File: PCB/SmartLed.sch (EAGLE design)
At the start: 49 parts, among them IC2 DS1307, IC3 MEGA8-P, K1 G5LE, Q2 32.768khz, T1 BC337

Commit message: Refactor PCB design (several enhancements)
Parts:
- removed IC4: (no value), v-reg:78XXS
- removed LED4: (no value), led:LED3MM
- removed R9: 330, rcl:R-EU_0207/10
- added IC1: (no value), v-reg:79XXL
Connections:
- removed net N$19: LED4.A, R9.1
- net +12V: now also IC1.IN; no longer IC4.IN
- net +5V: now also IC1.OUT; no longer IC4.OUT
- net GND: now also IC1.GND; no longer IC4.GND
- net N$6: no longer R9.2
- net N$7: no longer LED4.C
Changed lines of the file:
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@@
 <part name="R8" library="rcl" deviceset="R-EU_" device="0207/10" value="1.2k"/>
 <part name="GND10" library="supply1" deviceset="GND" device=""/>
-<part name="LED4" library="led" deviceset="LED" device="3MM"/>
-<part name="R9" library="rcl" deviceset="R-EU_" device="0207/10" value="330"/>
 <part name="LED5" library="led" deviceset="LED" device="3MM"/>
 <part name="R10" library="rcl" deviceset="R-EU_" device="0207/10" value="330"/>
@@
 <part name="C2" library="rcl" deviceset="C-EU" device="025-025X050" value="100nf"/>
 <part name="C7" library="rcl" deviceset="CPOL-EU" device="E2.5-5" value="4.7uf"/>
-<part name="IC4" library="v-reg" deviceset="78XXS" device=""/>
 <part name="GND8" library="supply1" deviceset="GND" device=""/>
 <part name="JP1" library="pinhead" deviceset="PINHD-1X5" device=""/>
@@
 <part name="P+11" library="supply1" deviceset="+5V" device=""/>
 <part name="Q2" library="crystal" deviceset="CRYSTAL" device="TC26V" value="32.768khz"/>
+<part name="IC1" library="v-reg" deviceset="79XXL" device=""/>
 </parts>
 <sheets>
@@
 <instance part="R8" gate="G$1" x="254" y="53.34"/>
 <instance part="GND10" gate="1" x="276.86" y="50.8"/>
-<instance part="LED4" gate="G$1" x="-73.66" y="73.66" rot="R270"/>
-<instance part="R9" gate="G$1" x="-63.5" y="73.66"/>
 <instance part="LED5" gate="G$1" x="190.5" y="15.24" rot="R90"/>
 <instance part="R10" gate="G$1" x="180.34" y="15.24"/>
@@
 <instance part="C2" gate="G$1" x="175.26" y="172.72" rot="MR180"/>
 <instance part="C7" gate="G$1" x="40.64" y="78.74" rot="R180"/>
-<instance part="IC4" gate="1" x="-5.08" y="111.76"/>
 <instance part="GND8" gate="1" x="175.26" y="165.1"/>
 <instance part="JP1" gate="A" x="132.08" y="35.56"/>
@@
 <instance part="P+11" gate="1" x="68.58" y="177.8"/>
 <instance part="Q2" gate="G$1" x="182.88" y="154.94" rot="R90"/>
+<instance part="IC1" gate="A" x="-5.08" y="111.76" rot="MR180"/>
 </instances>
 <busses>
@@
 <pinref part="OK1" gate="A" pin="A"/>
 <wire x1="-53.34" y1="58.42" x2="-53.34" y2="60.96" width="0.1524" layer="91"/>
-<wire x1="-53.34" y1="60.96" x2="-58.42" y2="60.96" width="0.1524" layer="91"/>
-<pinref part="R9" gate="G$1" pin="2"/>
-<wire x1="-58.42" y1="60.96" x2="-63.5" y2="60.96" width="0.1524" layer="91"/>
-<wire x1="-58.42" y1="73.66" x2="-58.42" y2="60.96" width="0.1524" layer="91"/>
+<wire x1="-53.34" y1="60.96" x2="-63.5" y2="60.96" width="0.1524" layer="91"/>
 <junction x="-73.66" y="60.96"/>
 <junction x="-63.5" y="60.96"/>
-<junction x="-58.42" y="60.96"/>
 </segment>
 </net>
@@
 <pinref part="R5-0.25W" gate="G$1" pin="2"/>
 <wire x1="-63.5" y1="48.26" x2="-73.66" y2="48.26" width="0.1524" layer="91"/>
-<wire x1="-73.66" y1="48.26" x2="-78.74" y2="48.26" width="0.1524" layer="91"/>
-<wire x1="-78.74" y1="48.26" x2="-111.76" y2="48.26" width="0.1524" layer="91"/>
+<wire x1="-73.66" y1="48.26" x2="-111.76" y2="48.26" width="0.1524" layer="91"/>
 <wire x1="-111.76" y1="48.26" x2="-111.76" y2="55.88" width="0.1524" layer="91"/>
 <pinref part="B1" gate="1" pin="-"/>
@@
 <pinref part="OK1" gate="A" pin="C"/>
 <wire x1="-53.34" y1="48.26" x2="-53.34" y2="53.34" width="0.1524" layer="91"/>
-<pinref part="LED4" gate="G$1" pin="C"/>
-<wire x1="-78.74" y1="73.66" x2="-78.74" y2="48.26" width="0.1524" layer="91"/>
-<junction x="-78.74" y="48.26"/>
 <junction x="-63.5" y="48.26"/>
 </segment>
@@
 <pinref part="P+2" gate="1" pin="+5V"/>
 <wire x1="12.7" y1="119.38" x2="12.7" y2="111.76" width="0.1524" layer="91"/>
-<wire x1="12.7" y1="111.76" x2="2.54" y2="111.76" width="0.1524" layer="91"/>
-<pinref part="IC4" gate="1" pin="OUT"/>
+<pinref part="IC1" gate="A" pin="OUT"/>
+<wire x1="2.54" y1="111.76" x2="12.7" y2="111.76" width="0.1524" layer="91"/>
 </segment>
 <segment>
@@
 <pinref part="GND2" gate="1" pin="GND"/>
 <wire x1="-5.08" y1="104.14" x2="-5.08" y2="101.6" width="0.1524" layer="91"/>
-<pinref part="IC4" gate="1" pin="GND"/>
+<pinref part="IC1" gate="A" pin="GND"/>
 </segment>
 <segment>
@@
 <net name="+12V" class="1">
 <segment>
-<wire x1="-12.7" y1="111.76" x2="-20.32" y2="111.76" width="0.1524" layer="91"/>
 <pinref part="12V" gate="-1" pin="KL"/>
 <wire x1="-20.32" y1="111.76" x2="-33.02" y2="111.76" width="0.1524" layer="91"/>
@@
 <pinref part="P+6" gate="1" pin="+12V"/>
 <wire x1="-20.32" y1="119.38" x2="-20.32" y2="111.76" width="0.1524" layer="91"/>
-<junction x="-20.32" y="111.76"/>
-<pinref part="IC4" gate="1" pin="IN"/>
+<pinref part="IC1" gate="A" pin="IN"/>
+<wire x1="-20.32" y1="111.76" x2="-12.7" y2="111.76" width="0.1524" layer="91"/>
 </segment>
 <segment>
@@
 </segment>
 </net>
-<net name="N$19" class="0">
-<segment>
-<pinref part="R9" gate="G$1" pin="1"/>
-<pinref part="LED4" gate="G$1" pin="A"/>
-<wire x1="-68.58" y1="73.66" x2="-71.12" y2="73.66" width="0.1524" layer="91"/>
-</segment>
-</net>

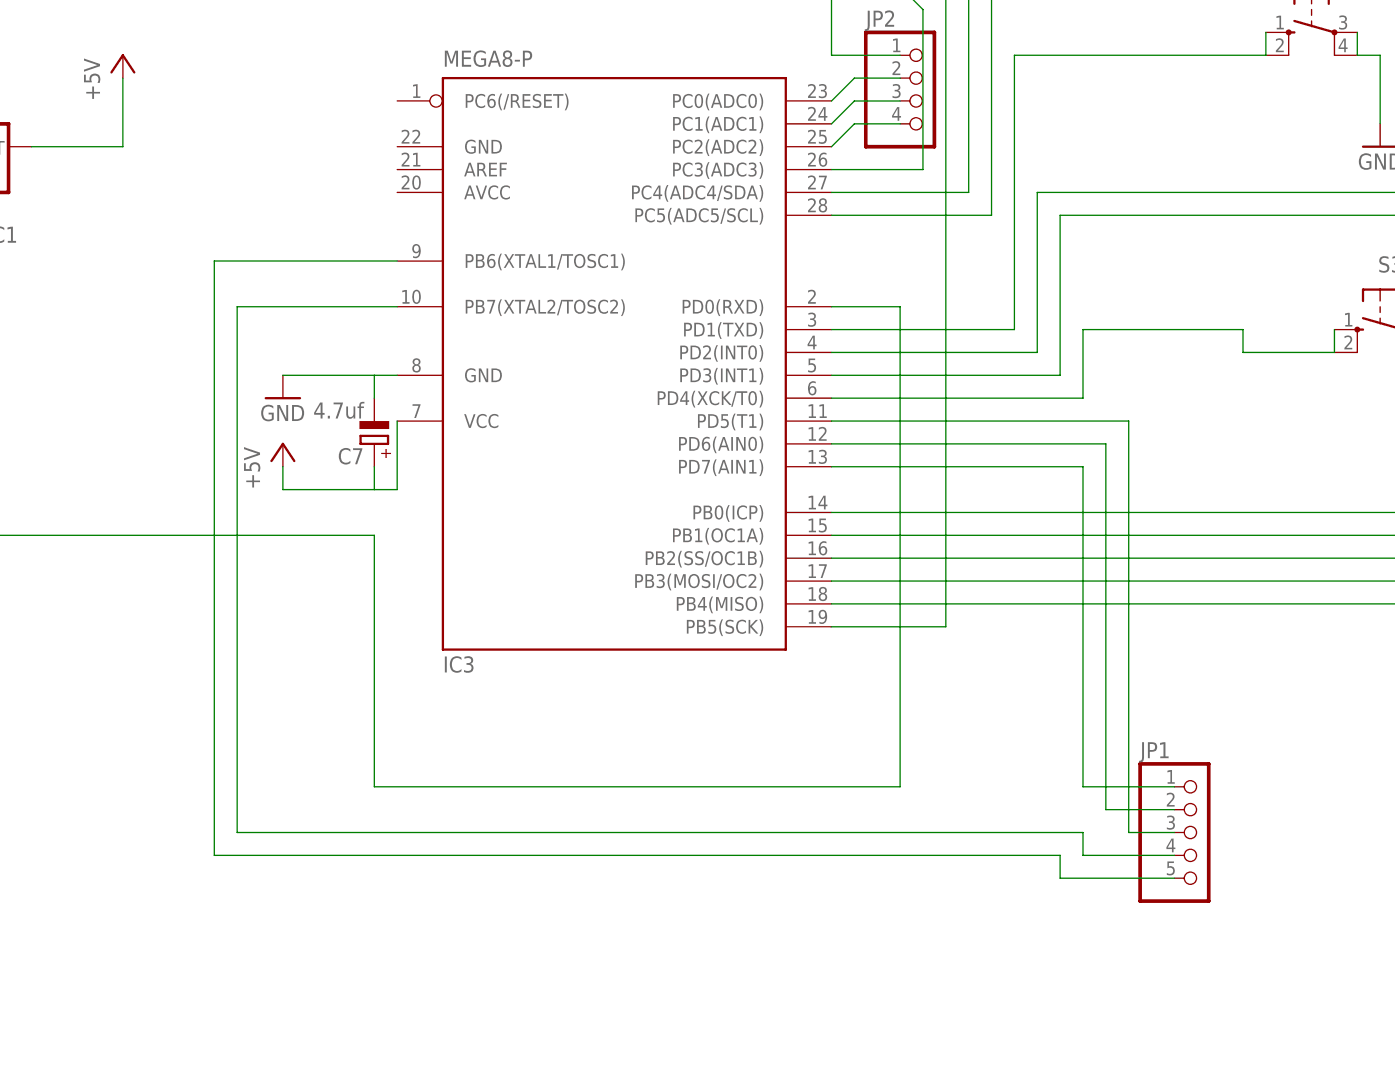
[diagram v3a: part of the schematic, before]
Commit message: Add PIR sensor pins to PCB
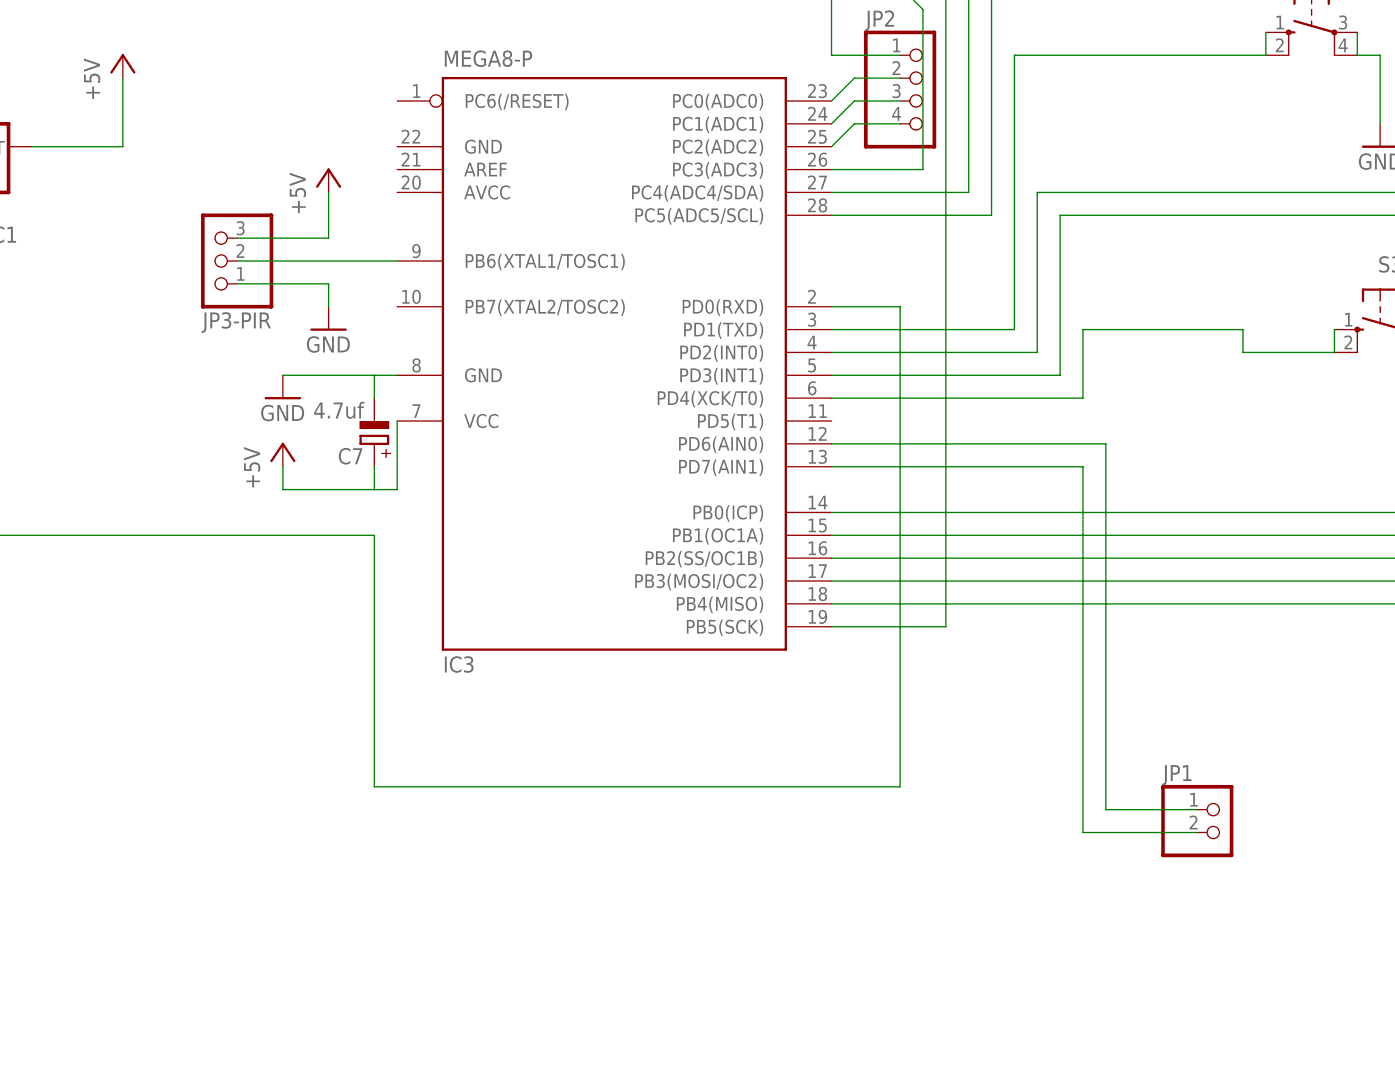
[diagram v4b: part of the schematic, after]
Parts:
- added JP3-PIR: (no value), pinhead:PINHD-1X3
- JP1: device pinhead:PINHD-1X5 -> pinhead:PINHD-1X2
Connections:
- removed net N$35: IC3.PD5(T1), JP1.3
- removed net N$41: IC3.PB6(XTAL1/TOSC1), JP1.5
- removed net N$42: IC3.PB7(XTAL2/TOSC2), JP1.4
- new net N$19: IC3.PB6(XTAL1/TOSC1), JP3-PIR.2
- net +5V: now also JP3-PIR.3
- net GND: now also JP3-PIR.1
- net N$37: now also JP1.1; no longer JP1.2
- net N$39: now also JP1.2; no longer JP1.1
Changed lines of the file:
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@@
 <part name="C7" library="rcl" deviceset="CPOL-EU" device="E2.5-5" value="4.7uf"/>
 <part name="GND8" library="supply1" deviceset="GND" device=""/>
-<part name="JP1" library="pinhead" deviceset="PINHD-1X5" device=""/>
 <part name="C1" library="rcl" deviceset="CPOL-EU" device="E2.5-5" value="4.7uf"/>
 <part name="C4" library="rcl" deviceset="C-EU" device="025-025X050" value="100nf"/>
@@
 <part name="Q2" library="crystal" deviceset="CRYSTAL" device="TC26V" value="32.768khz"/>
 <part name="IC1" library="v-reg" deviceset="79XXL" device=""/>
+<part name="JP3-PIR" library="pinhead" deviceset="PINHD-1X3" device=""/>
+<part name="P+12" library="supply1" deviceset="+5V" device=""/>
+<part name="GND17" library="supply1" deviceset="GND" device=""/>
+<part name="JP1" library="pinhead" deviceset="PINHD-1X2" device=""/>
 </parts>
 <sheets>
@@
 <instance part="C7" gate="G$1" x="40.64" y="78.74" rot="R180"/>
 <instance part="GND8" gate="1" x="175.26" y="165.1"/>
-<instance part="JP1" gate="A" x="132.08" y="35.56"/>
 <instance part="C1" gate="G$1" x="-25.4" y="58.42"/>
 <instance part="C4" gate="G$1" x="223.52" y="193.04" rot="MR90"/>
@@
 <instance part="Q2" gate="G$1" x="182.88" y="154.94" rot="R90"/>
 <instance part="IC1" gate="A" x="-5.08" y="111.76" rot="MR180"/>
+<instance part="JP3-PIR" gate="A" x="22.86" y="99.06" rot="R180"/>
+<instance part="P+12" gate="1" x="35.56" y="109.22"/>
+<instance part="GND17" gate="1" x="35.56" y="91.44"/>
+<instance part="JP1" gate="G$1" x="134.62" y="35.56"/>
 </instances>
 <busses>
@@
 <pinref part="R1" gate="G$1" pin="2"/>
 <wire x1="68.58" y1="175.26" x2="68.58" y2="170.18" width="0.1524" layer="91"/>
+</segment>
+<segment>
+<pinref part="P+12" gate="1" pin="+5V"/>
+<wire x1="35.56" y1="106.68" x2="35.56" y2="101.6" width="0.1524" layer="91"/>
+<pinref part="JP3-PIR" gate="A" pin="3"/>
+<wire x1="35.56" y1="101.6" x2="25.4" y2="101.6" width="0.1524" layer="91"/>
 </segment>
 </net>
@@
 <wire x1="71.12" y1="149.86" x2="78.74" y2="149.86" width="0.1524" layer="91"/>
 </segment>
+<segment>
+<pinref part="GND17" gate="1" pin="GND"/>
+<wire x1="35.56" y1="93.98" x2="35.56" y2="96.52" width="0.1524" layer="91"/>
+<pinref part="JP3-PIR" gate="A" pin="1"/>
+<wire x1="35.56" y1="96.52" x2="25.4" y2="96.52" width="0.1524" layer="91"/>
+</segment>
 </net>
 <net name="N$12" class="0">
@@
 </segment>
 </net>
-<net name="N$35" class="0">
-<segment>
-<pinref part="IC3" gate="G$1" pin="PD5(T1)"/>
-<wire x1="124.46" y1="81.28" x2="91.44" y2="81.28" width="0.1524" layer="91"/>
-<pinref part="JP1" gate="A" pin="3"/>
-<wire x1="129.54" y1="35.56" x2="124.46" y2="35.56" width="0.1524" layer="91"/>
-<wire x1="124.46" y1="35.56" x2="124.46" y2="81.28" width="0.1524" layer="91"/>
-</segment>
-</net>
 <net name="N$37" class="0">
 <segment>
 <pinref part="IC3" gate="G$1" pin="PD6(AIN0)"/>
 <wire x1="91.44" y1="78.74" x2="121.92" y2="78.74" width="0.1524" layer="91"/>
-<pinref part="JP1" gate="A" pin="2"/>
-<wire x1="129.54" y1="38.1" x2="121.92" y2="38.1" width="0.1524" layer="91"/>
 <wire x1="121.92" y1="38.1" x2="121.92" y2="78.74" width="0.1524" layer="91"/>
+<pinref part="JP1" gate="G$1" pin="1"/>
+<wire x1="132.08" y1="38.1" x2="121.92" y2="38.1" width="0.1524" layer="91"/>
 </segment>
 </net>
@@
 <pinref part="IC3" gate="G$1" pin="PD7(AIN1)"/>
 <wire x1="119.38" y1="76.2" x2="91.44" y2="76.2" width="0.1524" layer="91"/>
-<pinref part="JP1" gate="A" pin="1"/>
-<wire x1="129.54" y1="40.64" x2="119.38" y2="40.64" width="0.1524" layer="91"/>
-<wire x1="119.38" y1="40.64" x2="119.38" y2="76.2" width="0.1524" layer="91"/>
-</segment>
-</net>
-<net name="N$41" class="0">
-<segment>
-<pinref part="IC3" gate="G$1" pin="PB6(XTAL1/TOSC1)"/>
-<wire x1="43.18" y1="99.06" x2="22.86" y2="99.06" width="0.1524" layer="91"/>
-<wire x1="22.86" y1="99.06" x2="22.86" y2="33.02" width="0.1524" layer="91"/>
-<wire x1="116.84" y1="33.02" x2="22.86" y2="33.02" width="0.1524" layer="91"/>
-<wire x1="116.84" y1="33.02" x2="116.84" y2="30.48" width="0.1524" layer="91"/>
-<pinref part="JP1" gate="A" pin="5"/>
-<wire x1="116.84" y1="30.48" x2="129.54" y2="30.48" width="0.1524" layer="91"/>
-</segment>
-</net>
-<net name="N$42" class="0">
-<segment>
-<pinref part="JP1" gate="A" pin="4"/>
-<wire x1="129.54" y1="33.02" x2="119.38" y2="33.02" width="0.1524" layer="91"/>
-<wire x1="119.38" y1="33.02" x2="119.38" y2="35.56" width="0.1524" layer="91"/>
-<pinref part="IC3" gate="G$1" pin="PB7(XTAL2/TOSC2)"/>
-<wire x1="25.4" y1="93.98" x2="43.18" y2="93.98" width="0.1524" layer="91"/>
-<wire x1="25.4" y1="35.56" x2="25.4" y2="93.98" width="0.1524" layer="91"/>
-<wire x1="119.38" y1="35.56" x2="25.4" y2="35.56" width="0.1524" layer="91"/>
+<wire x1="119.38" y1="35.56" x2="119.38" y2="76.2" width="0.1524" layer="91"/>
+<pinref part="JP1" gate="G$1" pin="2"/>
+<wire x1="132.08" y1="35.56" x2="119.38" y2="35.56" width="0.1524" layer="91"/>
 </segment>
 </net>
@@
 </segment>
 </net>
+<net name="N$19" class="0">
+<segment>
+<pinref part="IC3" gate="G$1" pin="PB6(XTAL1/TOSC1)"/>
+<pinref part="JP3-PIR" gate="A" pin="2"/>
+<wire x1="43.18" y1="99.06" x2="25.4" y2="99.06" width="0.1524" layer="91"/>
+</segment>
+</net>

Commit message: Add a pinhead for light sensor
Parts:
- added JP3: (no value), pinhead:PINHD-1X2
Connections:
- net +5V: now also JP3.1
- net GND: now also JP3.2
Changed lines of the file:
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@@
 <part name="GND17" library="supply1" deviceset="GND" device=""/>
 <part name="JP1" library="pinhead" deviceset="PINHD-1X2" device=""/>
+<part name="JP3" library="pinhead" deviceset="PINHD-1X2" device=""/>
+<part name="GND18" library="supply1" deviceset="GND" device=""/>
+<part name="P+13" library="supply1" deviceset="+5V" device=""/>
 </parts>
 <sheets>
@@
 <instance part="GND17" gate="1" x="35.56" y="91.44"/>
 <instance part="JP1" gate="G$1" x="134.62" y="35.56"/>
+<instance part="JP3" gate="G$1" x="-68.58" y="88.9"/>
+<instance part="GND18" gate="1" x="-81.28" y="78.74"/>
+<instance part="P+13" gate="1" x="-81.28" y="99.06"/>
 </instances>
 <busses>
@@
 <pinref part="JP3-PIR" gate="A" pin="3"/>
 <wire x1="35.56" y1="101.6" x2="25.4" y2="101.6" width="0.1524" layer="91"/>
+</segment>
+<segment>
+<pinref part="P+13" gate="1" pin="+5V"/>
+<wire x1="-81.28" y1="96.52" x2="-81.28" y2="91.44" width="0.1524" layer="91"/>
+<pinref part="JP3" gate="G$1" pin="1"/>
+<wire x1="-81.28" y1="91.44" x2="-71.12" y2="91.44" width="0.1524" layer="91"/>
 </segment>
 </net>
@@
 <wire x1="35.56" y1="96.52" x2="25.4" y2="96.52" width="0.1524" layer="91"/>
 </segment>
-</net>
+<segment>
+<pinref part="JP3" gate="G$1" pin="2"/>
+<pinref part="GND18" gate="1" pin="GND"/>
+<wire x1="-71.12" y1="88.9" x2="-81.28" y2="88.9" width="0.1524" layer="91"/>
+<wire x1="-81.28" y1="88.9" x2="-81.28" y2="81.28" width="0.1524" layer="91"/>
+</segment>
+</net>

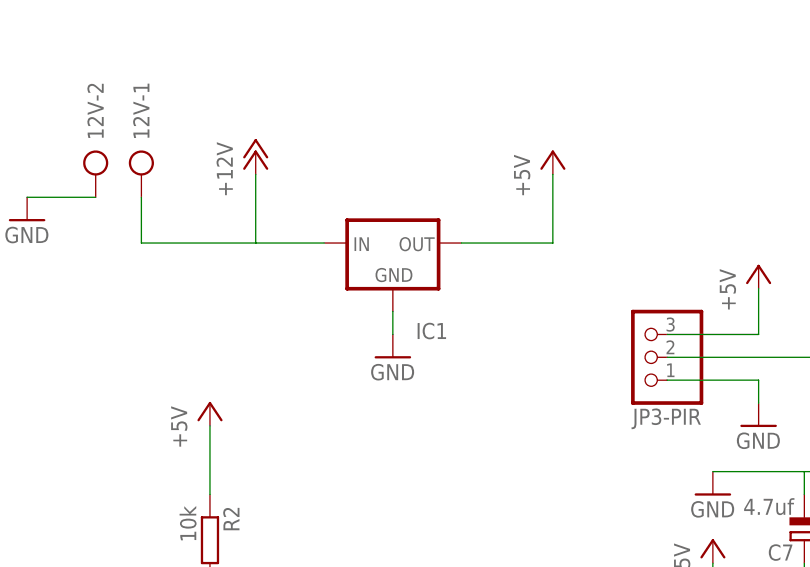
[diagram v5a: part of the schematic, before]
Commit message: Fix wrong voltage regulator footprint
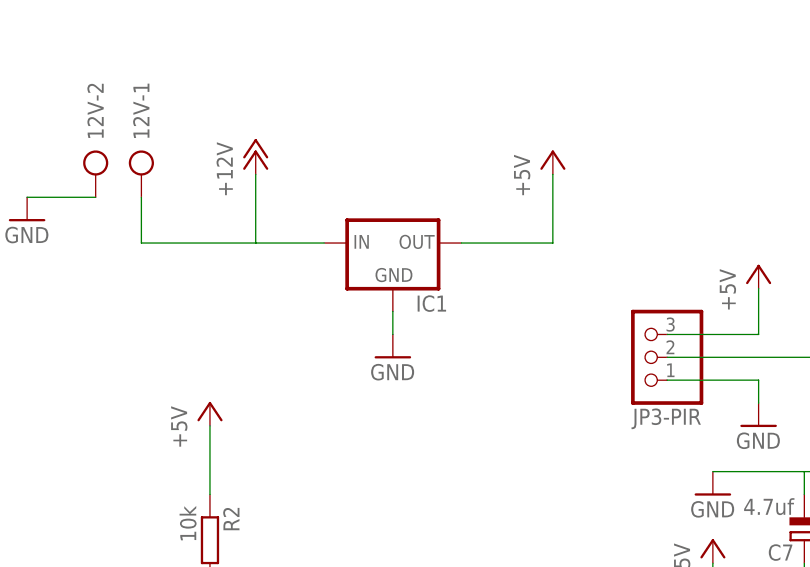
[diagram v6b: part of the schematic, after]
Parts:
- IC1: device v-reg:79XXL -> v-reg:78XXL
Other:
- moved on the sheet: IC1
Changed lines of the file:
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@@
 <part name="P+11" library="supply1" deviceset="+5V" device=""/>
 <part name="Q2" library="crystal" deviceset="CRYSTAL" device="TC26V" value="32.768khz"/>
-<part name="IC1" library="v-reg" deviceset="79XXL" device=""/>
 <part name="JP3-PIR" library="pinhead" deviceset="PINHD-1X3" device=""/>
 <part name="P+12" library="supply1" deviceset="+5V" device=""/>
@@
 <part name="GND18" library="supply1" deviceset="GND" device=""/>
 <part name="P+13" library="supply1" deviceset="+5V" device=""/>
+<part name="IC1" library="v-reg" deviceset="78XXL" device=""/>
 </parts>
 <sheets>
@@
 <instance part="P+11" gate="1" x="68.58" y="177.8"/>
 <instance part="Q2" gate="G$1" x="182.88" y="154.94" rot="R90"/>
-<instance part="IC1" gate="A" x="-5.08" y="111.76" rot="MR180"/>
 <instance part="JP3-PIR" gate="A" x="22.86" y="99.06" rot="R180"/>
 <instance part="P+12" gate="1" x="35.56" y="109.22"/>
@@
 <instance part="GND18" gate="1" x="-81.28" y="78.74"/>
 <instance part="P+13" gate="1" x="-81.28" y="99.06"/>
+<instance part="IC1" gate="A" x="-5.08" y="111.76"/>
 </instances>
 <busses>
@@
 <pinref part="P+2" gate="1" pin="+5V"/>
 <wire x1="12.7" y1="119.38" x2="12.7" y2="111.76" width="0.1524" layer="91"/>
+<wire x1="2.54" y1="111.76" x2="12.7" y2="111.76" width="0.1524" layer="91"/>
 <pinref part="IC1" gate="A" pin="OUT"/>
-<wire x1="2.54" y1="111.76" x2="12.7" y2="111.76" width="0.1524" layer="91"/>
 </segment>
 <segment>
@@
 <pinref part="P+6" gate="1" pin="+12V"/>
 <wire x1="-20.32" y1="119.38" x2="-20.32" y2="111.76" width="0.1524" layer="91"/>
+<wire x1="-20.32" y1="111.76" x2="-12.7" y2="111.76" width="0.1524" layer="91"/>
 <pinref part="IC1" gate="A" pin="IN"/>
-<wire x1="-20.32" y1="111.76" x2="-12.7" y2="111.76" width="0.1524" layer="91"/>
-</segment>
-<segment>
+</segment>
+<segment>
